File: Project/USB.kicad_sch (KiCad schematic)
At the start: 10 parts, among them J1 HRO_TYPE-C-31-M-14, U4 USBLC6-2P6

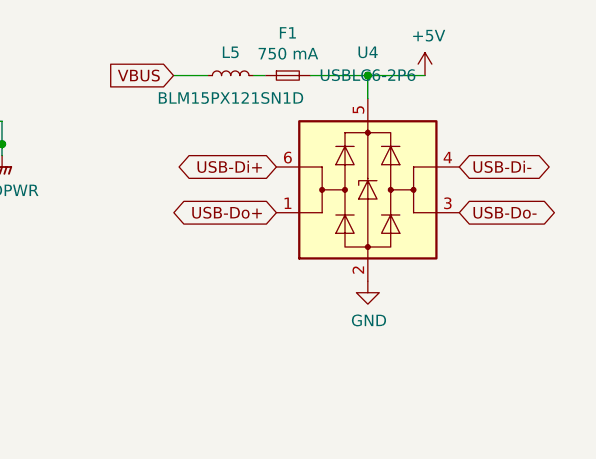
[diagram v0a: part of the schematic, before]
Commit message: switching to holyiot for BLE
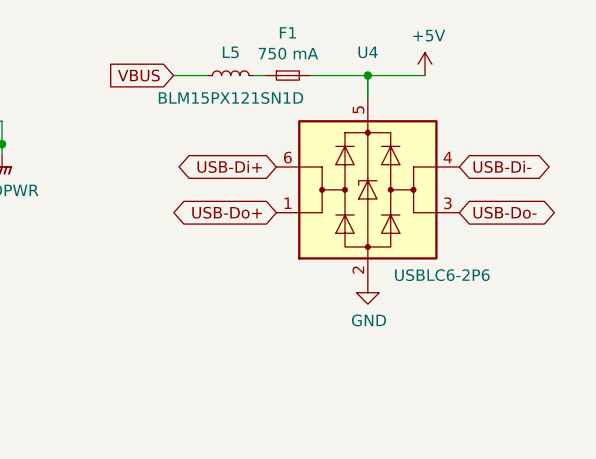
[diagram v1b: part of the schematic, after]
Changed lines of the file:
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@@
   )
   (symbol (lib_id "Device:L_Small") (at 97.79 24.13 90) (unit 1)
-    (in_bom yes) (on_board yes) (dnp no) (fields_autoplaced)
+    (in_bom yes) (on_board yes) (dnp no)
     (property "Reference" "L5" (at 97.79 21.59 90)
       (effects (font (size 1.27 1.27)))
@@
   )
   (symbol (lib_id "Power_Protection:USBLC6-2P6") (at 113.03 36.83 0) (unit 1)
-    (in_bom yes) (on_board yes) (dnp no) (fields_autoplaced)
+    (in_bom yes) (on_board yes) (dnp no)
     (property "Reference" "U4" (at 113.03 21.59 0)
       (effects (font (size 1.27 1.27)))
     )
-    (property "Value" "USBLC6-2P6" (at 113.03 24.13 0)
-      (effects (font (size 1.27 1.27)))
-    )
+    (property "Value" "USBLC6-2P6" (at 121.285 46.355 0)
+      (effects (font (size 1.27 1.27)))
+    )

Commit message: BLE progress
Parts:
- removed C28: 100 nF, Capacitor_SMD:C_0402_1005Metric, symbol Device:C_Small
- removed D43: BSD3C051V, Diode_SMD:D_SOD-323, symbol Device:D_TVS
- removed L6: BLM15PX121SN1D, Inductor_SMD:L_0402_1005Metric, symbol Device:L_Small
- removed R12, R13: 5.1 kOhm, Resistor_SMD:R_0402_1005Metric, symbol Device:R_Small
- removed R14: 1 MOhm, Resistor_SMD:R_0402_1005Metric, symbol Device:R_Small
- added R4, R5: 5.1k, Resistor_SMD:R_0402_1005Metric, symbol Device:R_Small
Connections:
- net Earth is gone; now on net GND: J1.S1 (SHIELD)
- net GNDPWR is gone; now on net GND: J1.A1 (GND), J1.A12 (GND), J1.B1 (GND), J1.B12 (GND)
- net GND: now also R4.2, R5.2
- net CC2: now reaches J1.B5 (CC2)
- net CC2: now also R5.1
- net CC1: now reaches J1.A5 (CC1)
- net CC1: now also R4.1
- net USB-Di+ renamed DATA ESD+
- net USB-Di- renamed DATA ESD-
- net USB-Do+ renamed DATA+
- net USB-Do- renamed DATA-
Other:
- moved on the sheet: F1, L5, U4
